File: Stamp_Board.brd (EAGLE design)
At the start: 100 x 80 mm, 15 parts

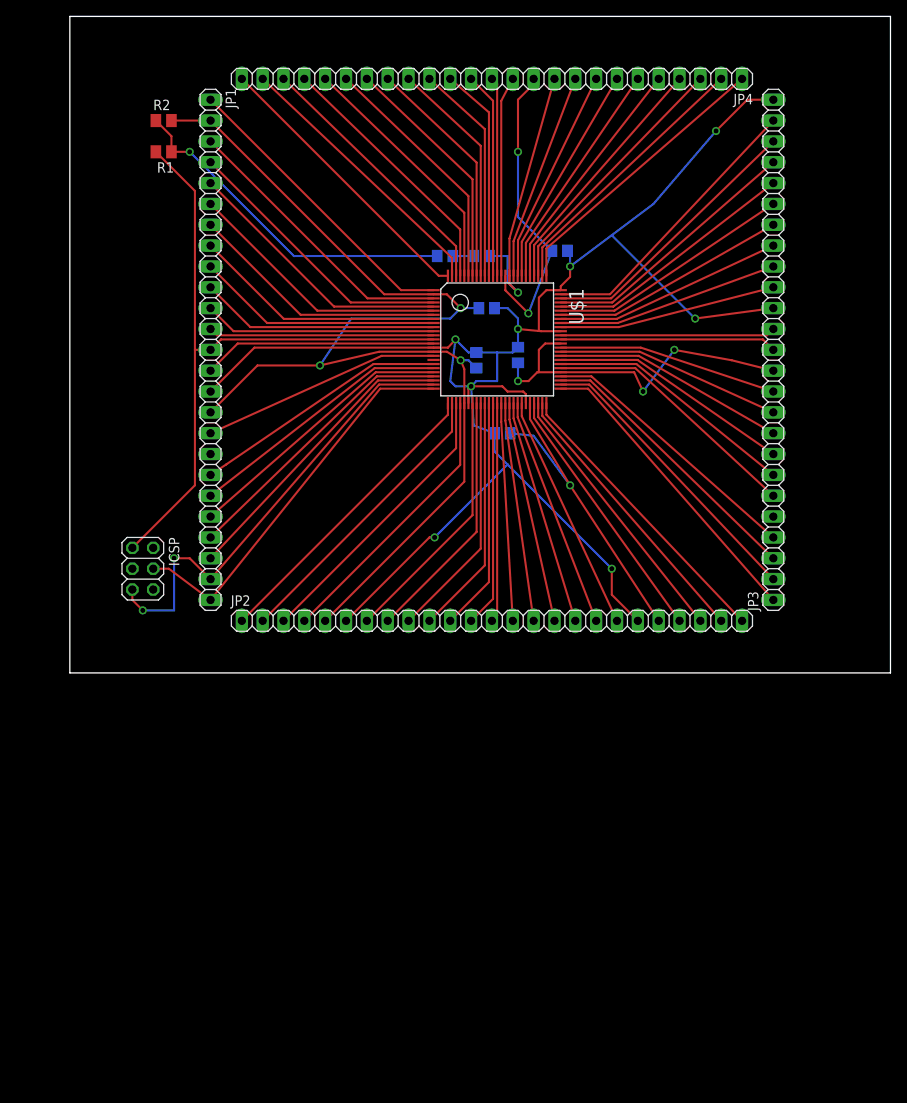
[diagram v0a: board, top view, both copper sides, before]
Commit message: Added oscillator schematic to Stamp Board and started layout corrections.
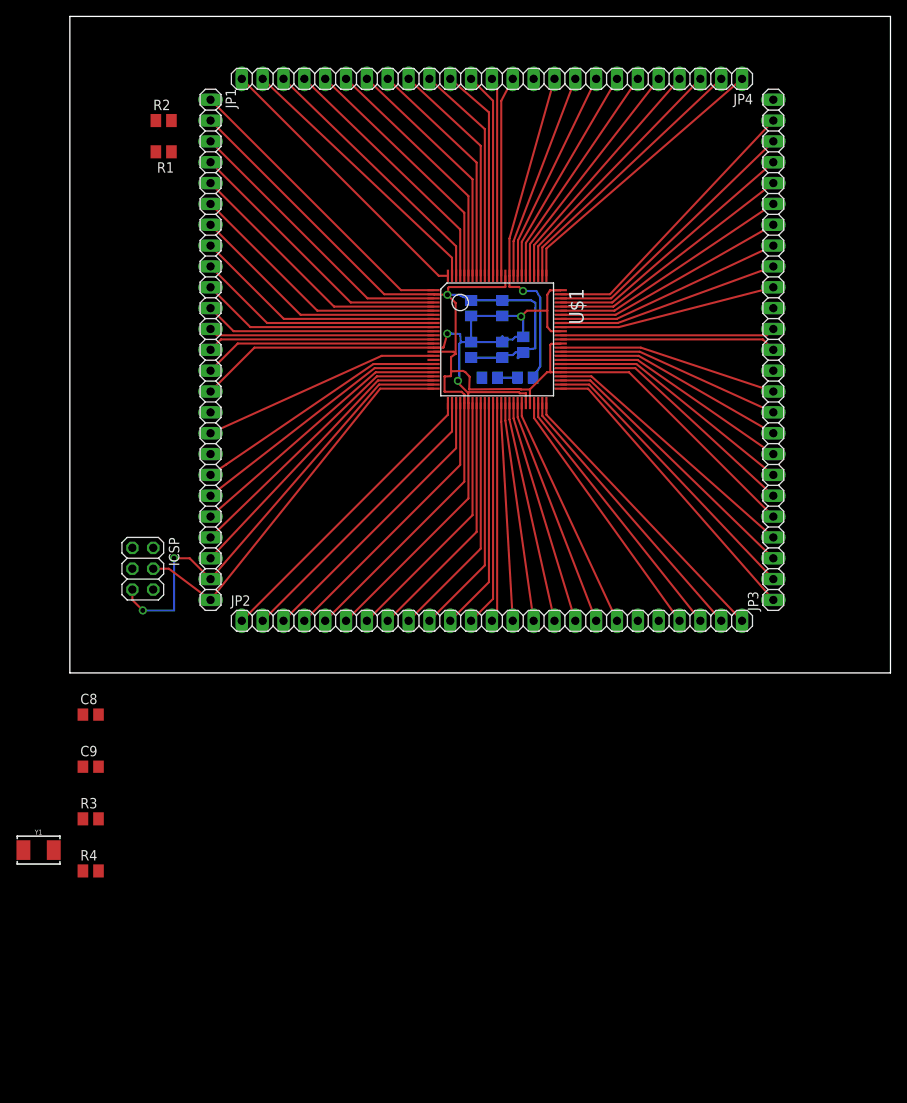
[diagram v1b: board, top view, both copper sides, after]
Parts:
- added C8, C9: (no value), rcl:C0805
- added R3, R4: (no value), rcl:M0805
- added Y1: (no value), SparkFun-Clocks:CRYSTAL-SMD-5X3.2-2PAD
- moved C6 16.2 mm to (48.9, 39.4), turned to 90 degrees
- moved C1 15.8 mm to (51.2, 36.0)
- moved C7 15.7 mm to (55.5, 36.0)
- moved C4 10.2 mm to (52.7, 39.4), turned to 90 degrees
- moved C3 7.10 mm to (52.7, 44.5), turned to 270 degrees
- moved C2 1.90 mm to (48.9, 44.5), turned to 90 degrees
- moved C5 1.42 mm to (55.2, 40.0)
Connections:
- removed net N$10: C6.1, JP4.11, U$1.86
- removed net N$42: JP2.1, U$1.26
- removed net N$43: JP2.2, U$1.27
- removed net N$7: C4.1, JP2.21, U$1.46
- removed net N$9: C5.2, JP3.12, JP3.5, U$1.55, U$1.62
- new net GND: C8.1, C9.1
- new net N$11: JP3.14, R3.1, U$1.64
- new net N$15: JP3.13, R4.1, U$1.63
- new net N$6: C8.2, R3.2, Y1.P$2
- new net N$8: C9.2, R4.2, Y1.P$1
- net FRET16: now also JP2.1, U$1.26; no longer JP3.13, U$1.63
- net FRET17: now also JP2.2, U$1.27; no longer JP3.14, U$1.64
- net VDD: now also C4.1, C5.2, C6.1, JP2.21, JP3.12, JP3.5, JP4.11, U$1.46, U$1.55, U$1.62, U$1.86
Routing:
- net VSS: track 212.9 -> 115.8 mm, vias 8 -> 3
- net N$13: track 83.0 -> 27.7 mm
- net N$9: track 43.8 -> 0.00 mm, vias 3 -> 0
- net N$1: track 42.2 -> 0.00 mm, vias 1 -> 0
- net N$7: track 41.5 -> 0.00 mm, vias 1 -> 0
- net VDD: track 142.2 -> 181.7 mm, vias 3 -> 1
- net N$10: track 37.3 -> 0.00 mm, vias 2 -> 0
- net N$42: track 36.9 -> 0.00 mm
- net N$43: track 36.1 -> 0.00 mm
- net N$15: track 0.00 -> 26.4 mm
- net N$11: track 0.00 -> 26.2 mm
- net FRET16: track 26.4 -> 36.9 mm
- net FRET17: track 26.2 -> 36.1 mm
- net N$12: track 34.4 -> 40.5 mm

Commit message: Completed stamp board layout
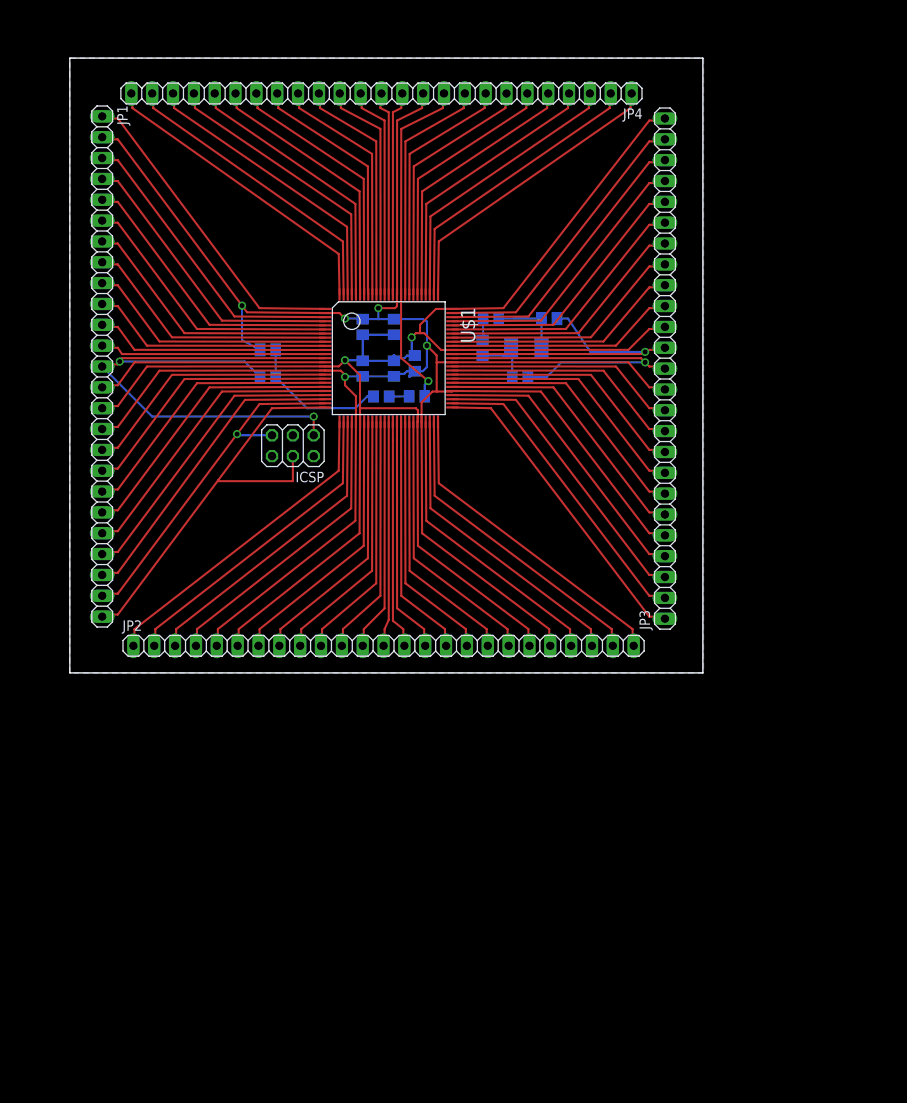
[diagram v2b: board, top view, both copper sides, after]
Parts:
- moved Y1 85.3 mm to (55.6, 39.6), flipped to the bottom
- moved R3 82.7 mm to (58.4, 43.2), flipped to the bottom
- moved R4 79.8 mm to (54.9, 36.1), flipped to the bottom
- moved C9 69.9 mm to (50.3, 39.6), flipped to the bottom, turned to 270 degrees
- moved C8 68.6 mm to (51.3, 43.2), flipped to the bottom, turned to 180 degrees
- moved R2 30.7 mm to (24.1, 39.4), flipped to the bottom
- moved R1 30.2 mm to (24.1, 36.1), flipped to the bottom, turned to 0 degrees
- moved ICSP 23.6 mm to (27.2, 27.7), turned to 180 degrees
- moved JP4 13.6 mm to (39.2, 70.6)
- moved JP2 13.6 mm to (37.0, 3.30)
- moved C2 13.4 mm to (35.7, 42.2)
- moved C6 13.4 mm to (35.7, 37.1)
- moved C7 13.4 mm to (42.3, 33.7)
- moved C1 13.4 mm to (38.0, 33.7)
- moved C3 13.4 mm to (39.5, 42.2)
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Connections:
- net P0_0 renamed P2_0
- removed net PE: C1.2, C7.1
- net GND: now also C1.2, C7.1
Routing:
- net VDD: track 181.7 -> 293.5 mm, vias 1 -> 5
- net VSS: track 115.8 -> 212.7 mm, vias 3 -> 2
- net N$13: track 27.7 -> 76.2 mm, vias 0 -> 2
- net P2_0: track 28.5 -> 61.5 mm
- net N$1: track 0.00 -> 17.4 mm
- net N$15: track 26.4 -> 41.5 mm, vias 0 -> 1
- net N$2: track 56.7 -> 43.2 mm, vias 2 -> 1
- net N$11: track 26.2 -> 39.0 mm, vias 0 -> 1
- net N$6: track 0.00 -> 8.77 mm
- net N$8: track 0.00 -> 7.49 mm
- net GND: track 0.00 -> 5.07 mm
- net N$14: track 47.8 -> 52.1 mm
- net FRET4: track 29.1 -> 33.0 mm
- net FRET5: track 32.2 -> 36.1 mm
- net FRET3: track 28.3 -> 32.0 mm
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- added copper zone on layer 16, net GND
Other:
- board size 100 x 80 mm -> 77.1 x 74.9 mm

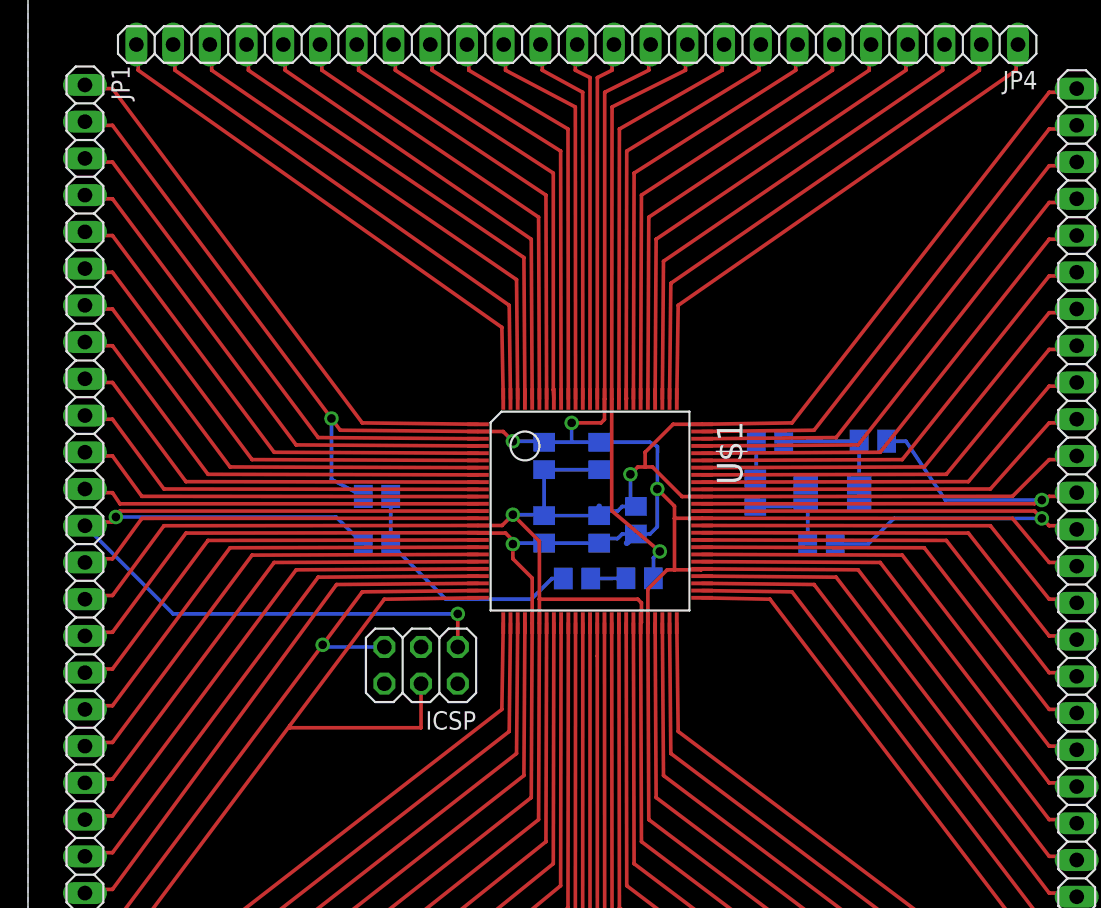
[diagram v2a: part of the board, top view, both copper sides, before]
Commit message: Completed traces to other PCBs
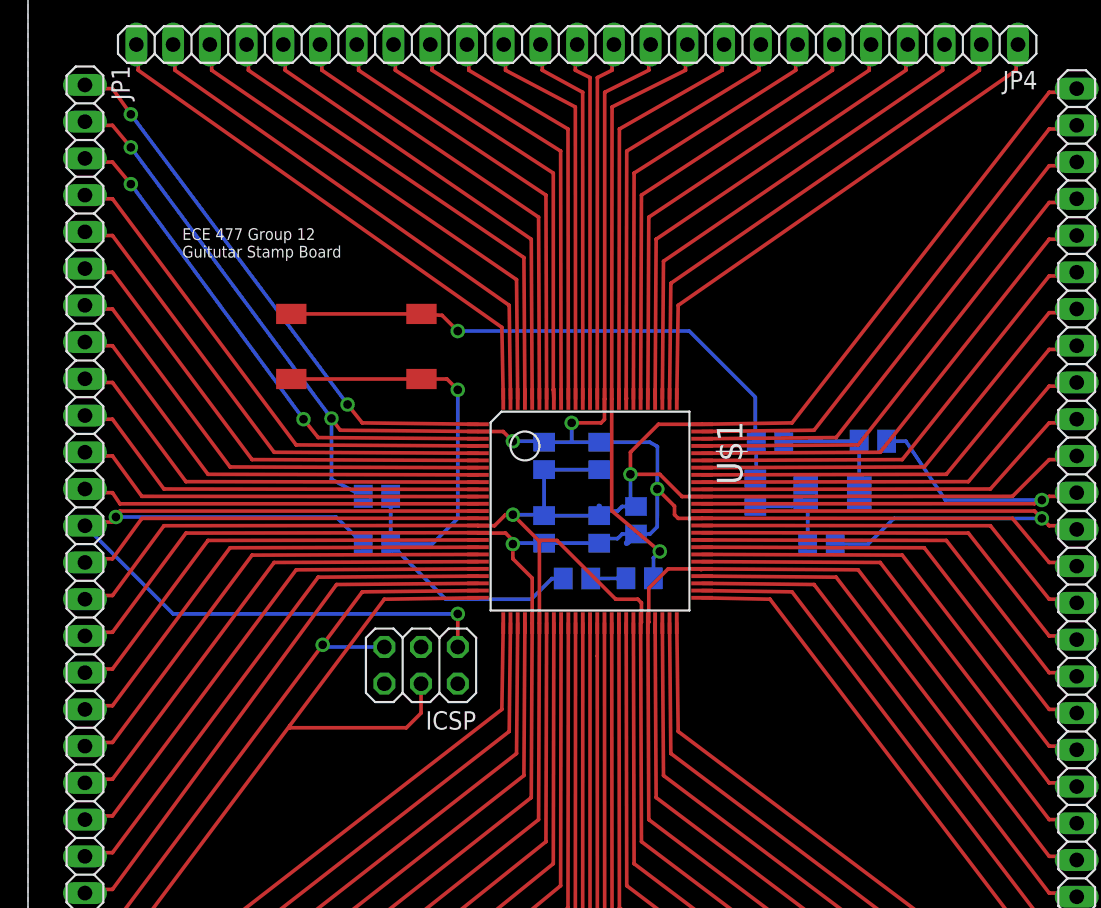
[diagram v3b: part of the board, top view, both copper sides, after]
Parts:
- added U$2: LL3301NF065QG, ECE477_Guitutar:LL3301NF065QG
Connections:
- removed net N$1: C1.1, R1.1, R2.1
- new net N$16: C1.1, R1.1, R2.1, U$2.P$3, U$2.P$4
- net GND: now also U$2.P$1, U$2.P$2
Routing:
- net N$16: track 0.00 -> 43.5 mm, vias 0 -> 1
- net GND: track 5.07 -> 42.6 mm, vias 0 -> 1
- net N$1: track 17.4 -> 0.00 mm
- net VDD: track 293.5 -> 289.9 mm, vias 5 -> 6
- net VSS: track 212.7 -> 215.5 mm
- net N$14: track 52.1 -> 51.6 mm
- net P0_4: vias 0 -> 2
- net P1_5: vias 0 -> 2
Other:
- board text added: "ECE 477 Group 12 Guitutar Stamp Board"

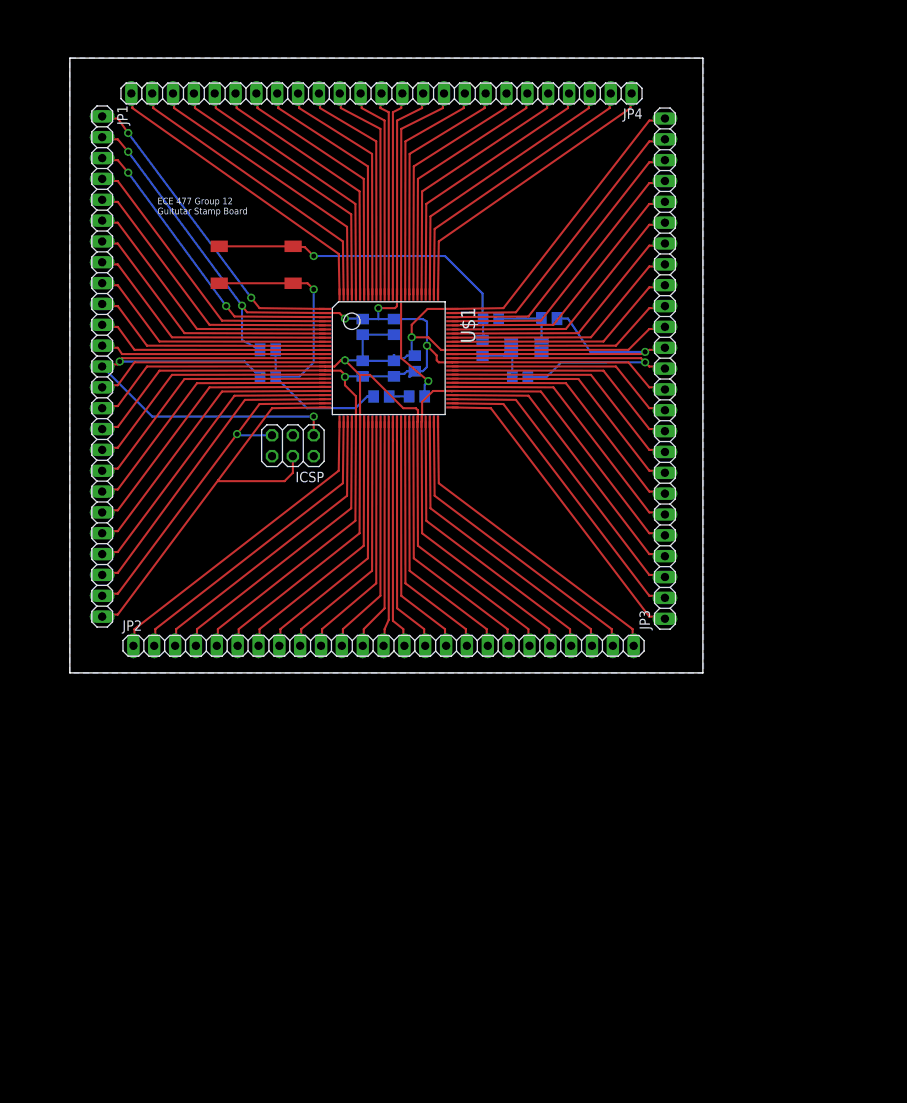
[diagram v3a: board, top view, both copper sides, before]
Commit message: Added more caps because of PIC32 recommended connection. Updated and finished PCB layout. Added LDO to regulate input voltage.
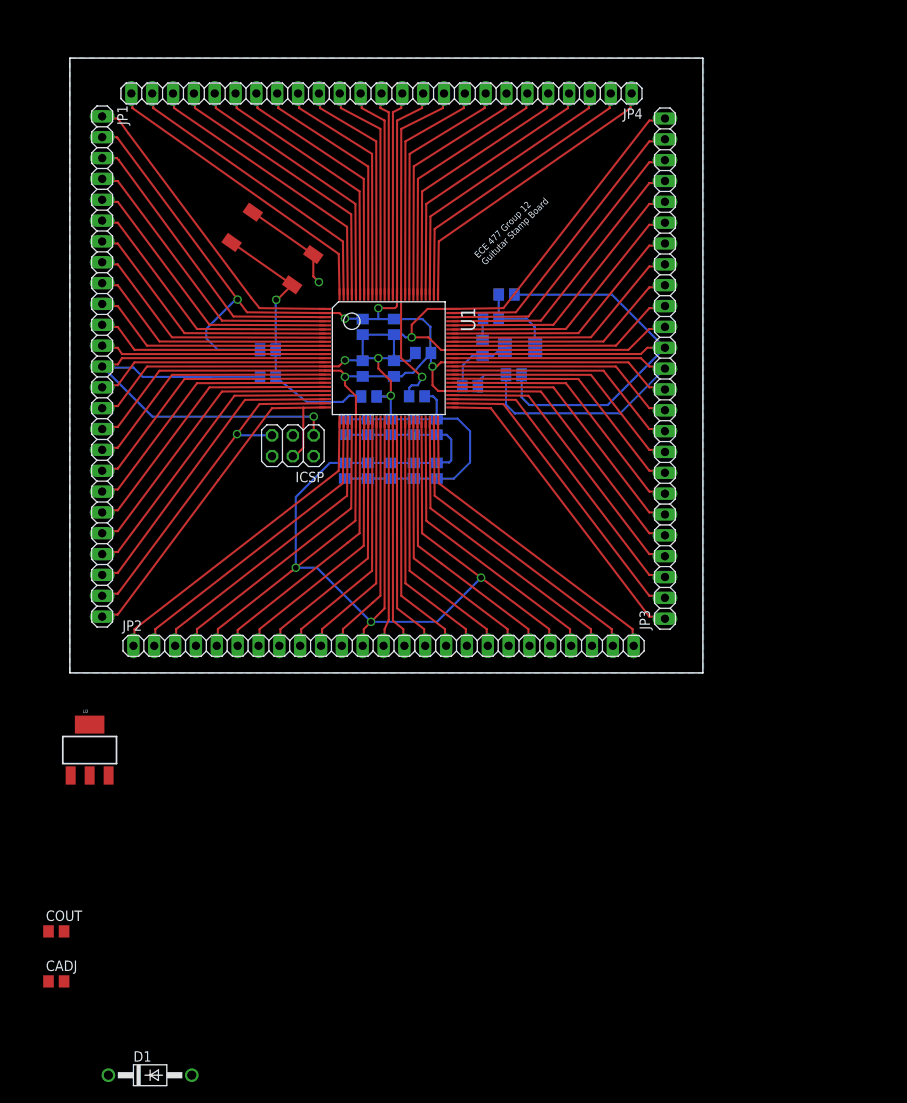
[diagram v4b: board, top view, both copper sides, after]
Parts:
- removed U$2: LL3301NF065QG, ECE477_Guitutar:LL3301NF065QG
- added C10, C11, C12, C13, C14, C15, C16: 0.01uF, rcl:C0805
- added C17, CADJ: 10uF, rcl:C0805
- added C18, C19: 9.1uF, rcl:C0805
- added COUT: 100uF, rcl:C0805
- added D1: 1N4004, diode:DO41-10
- added R5: 0.0, rcl:R0805
- added S1: LL3301NF065QG, ECE477_Guitutar:LL3301NF065QG
- added U2: (no value), SparkFun-IC-Power:SOT223
- C1, C2, C3, C4, C5, C6, C7, C8, C9: value (none) -> 0.1uF
- R1: value (none) -> 1k
- R2: value (none) -> 10k
- R3: value (none) -> 1M
- R4: value (none) -> 0.0; device rcl:M0805 -> rcl:R0805
- Y1: value (none) -> 16MHz
- moved C2 17.7 mm to (33.5, 24.6), turned to 270 degrees
- moved C3 17.5 mm to (39.1, 24.6), turned to 90 degrees
- moved C8 16.8 mm to (35.7, 37.1), turned to 90 degrees
- moved C6 15.4 mm to (44.7, 24.6), turned to 270 degrees
- moved C4 12.7 mm to (41.9, 24.6), turned to 270 degrees
- moved R4 10.2 mm to (53.2, 46.1)
- moved R3 8.10 mm to (54.1, 36.3), turned to 180 degrees
- moved C5 7.75 mm to (41.9, 30.0), turned to 90 degrees
- moved C9 7.27 mm to (43.1, 39.0), turned to 0 degrees
- moved C7 7.04 mm to (36.3, 30.0), turned to 90 degrees
- moved C1 1.52 mm to (36.4, 33.7)
- moved Y1 0.76 mm to (54.9, 39.6)
- renumbered U$1 to U1
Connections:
- removed net N$11: JP3.14, R3.1, U1.64
- removed net N$50: JP2.11, U1.36
- removed net N$51: JP2.12, U1.37
- removed net VSS: C2.1, C3.2, C4.2, C5.1, C6.2, JP1.15, JP2.20, JP2.6, JP3.15, JP3.25, U1.15, U1.31, U1.45, U1.65, U1.75
- new net 3.3V: COUT.1, D1.A, U2.2, U2.4
- new net 5.2V_PB: CADJ.1, D1.C, U2.3
- new net N$1: JP3.14, R3.2, R4.1, U1.64
- net GND: now also C10.2, C11.1, C12.2, C13.2, C14.2, C15.2, C16.2, C17.2, C18.2, C19.2, C2.2, C3.1, C4.2, C5.2, C6.2, C7.2, C8.2, C9.2, CADJ.2, COUT.2, JP1.15, JP2.11, JP2.20, JP2.6, JP3.15, JP3.25, S1.P$1, S1.P$2, U1.15, U1.31, U1.36, U1.45, U1.65, U1.75; no longer C7.1, C8.1, C9.1, U$2.P$1, U$2.P$2
- net N$12: now also C17.1; no longer C7.2
- net N$15: now also R3.1, R5.1; no longer R4.1
- net N$16: now also S1.P$3, S1.P$4; no longer U$2.P$3, U$2.P$4
- net N$6: now also C18.1, R4.2; no longer C8.2, R3.2
- net N$8: now also C19.1, R5.2; no longer C9.2, R4.2
- net VDD: now also C10.1, C11.2, C12.1, C13.1, C14.1, C15.1, C16.1, C2.1, C3.2, C5.1, C7.1, C8.1, C9.1, JP2.12, U1.37; no longer C2.2, C3.1, C5.2
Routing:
- net GND: track 42.6 -> 295.1 mm, vias 1 -> 5
- net VSS: track 215.5 -> 0.00 mm, vias 2 -> 0
- net VDD: track 289.9 -> 395.0 mm, vias 6 -> 8
- net N$1: track 0.00 -> 70.7 mm
- net N$11: track 39.0 -> 0.00 mm, vias 1 -> 0
- net N$50: track 29.4 -> 0.00 mm
- net N$51: track 28.4 -> 0.00 mm
- net N$15: track 41.5 -> 56.7 mm, vias 1 -> 0
- net N$16: track 43.5 -> 33.0 mm
- net N$14: track 51.6 -> 46.5 mm
- net N$13: track 76.2 -> 78.0 mm, vias 2 -> 1
- net N$6: track 8.77 -> 10.3 mm
- net N$8: track 7.49 -> 8.65 mm
- net P0_4: track 36.8 -> 36.9 mm, vias 2 -> 0
- net P1_5: vias 2 -> 0
